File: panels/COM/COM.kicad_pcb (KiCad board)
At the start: 2 copper layers, 71 x 132.5 mm, 4 parts

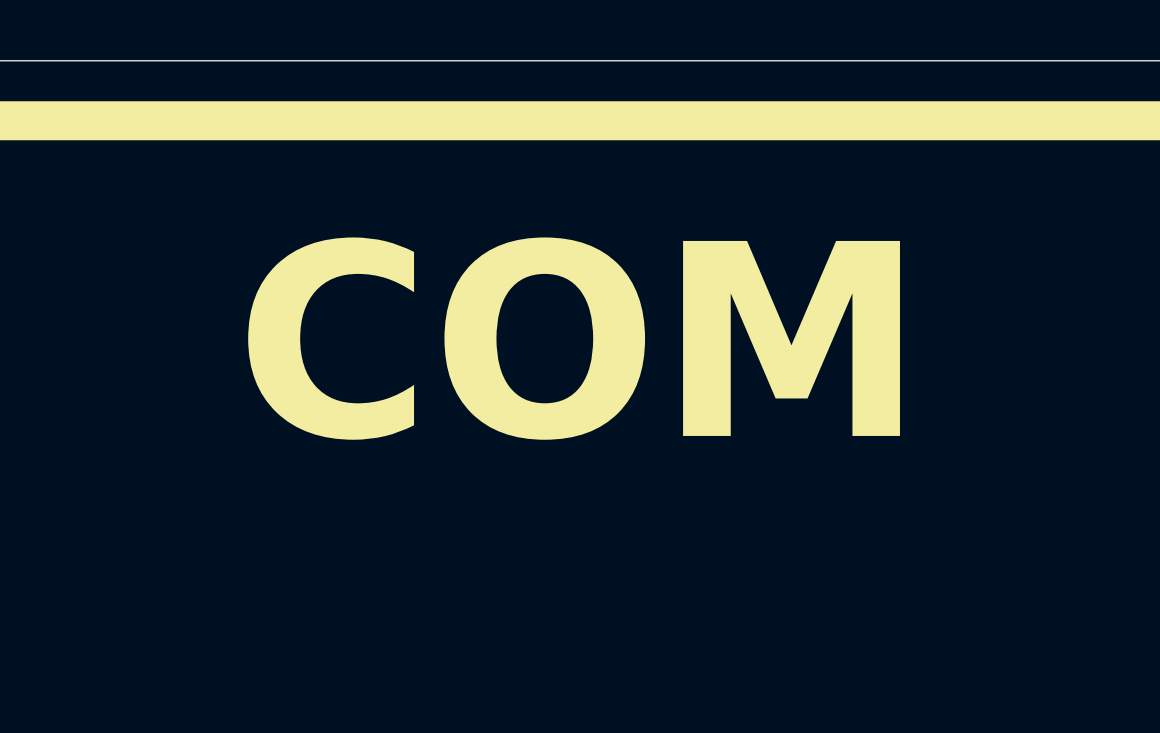
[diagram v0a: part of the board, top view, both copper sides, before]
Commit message: 3U panels initial version
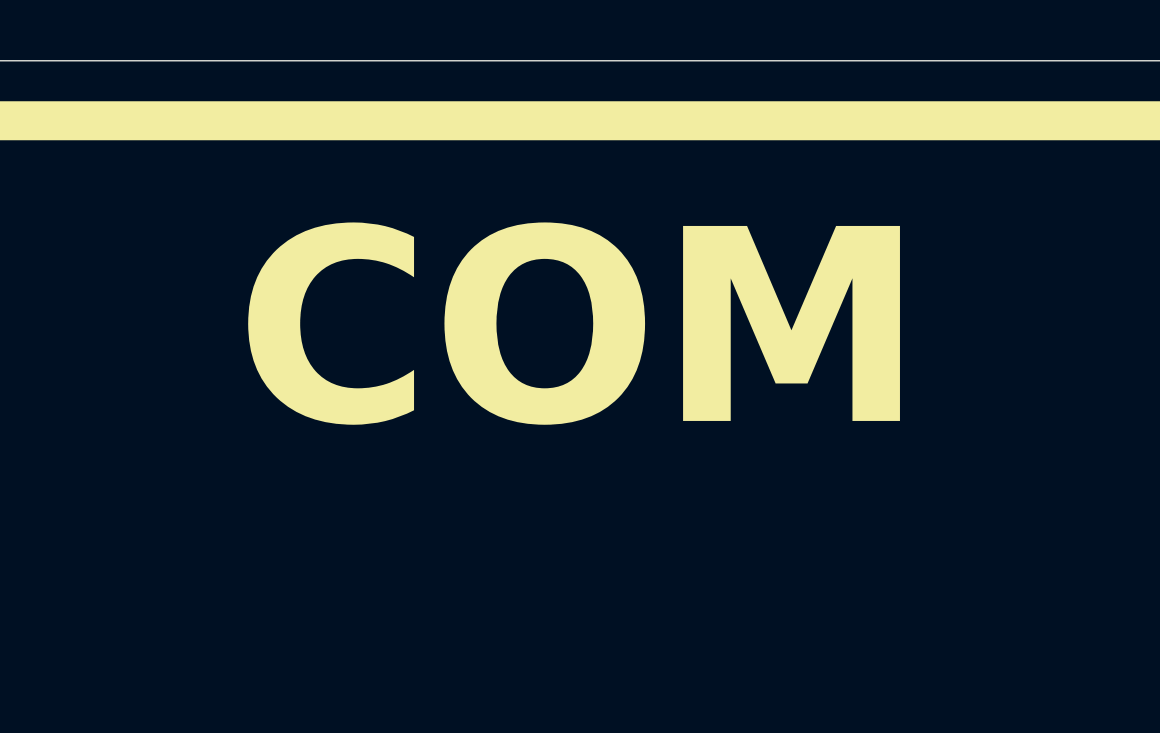
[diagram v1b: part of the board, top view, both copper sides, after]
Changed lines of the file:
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@@
 	)
 	(gr_text "COM"
-		(at 101.745894 44.915428 0)
+		(at 101.745894 44.415428 0)
 		(layer "F.SilkS")
 		(effects
@@
 			(polygon
 				(pts
-					(xy 94.889539 45.566539) (xy 94.851151 46.22562) (xy 94.751219 46.697101) (xy 94.607595 47.025142)
-					(xy 94.429935 47.245403) (xy 94.193747 47.403744) (xy 93.839887 47.53445) (xy 93.329149 47.626331)
-					(xy 92.614539 47.661746) (xy 91.203976 47.689131) (xy 90.057744 47.670874) (xy 89.246857 47.642712)
-					(xy 88.645545 47.56866) (xy 88.211816 47.462466) (xy 87.908803 47.33485) (xy 87.70535 47.192616)
-					(xy 87.488232 46.937991) (xy 87.325718 46.615743) (xy 87.220507 46.210524) (xy 87.182243 45.702277)
-					(xy 87.127471 44.426261) (xy 87.161982 43.648642) (xy 87.25475 43.044425) (xy 87.392067 42.582122)
-					(xy 87.564055 42.234212) (xy 87.754235 42.002544) (xy 88.010959 41.814211) (xy 88.348204 41.668833)
-					(xy 88.785705 41.572453) (xy 89.3477 41.536868) (xy 91.07697 41.491225) (xy 92.323616 41.505116)
-					(xy 93.51549 41.591242) (xy 93.853291 41.660521) (xy 94.125091 41.785758) (xy 94.343688 41.96481)
-					(xy 94.516459 42.202857) (xy 94.673885 42.575213) (xy 94.778324 43.057298) (xy 94.816908 43.675733)
-					(xy 93.024135 43.675733) (xy 92.996554 43.415026) (xy 92.925515 43.243628) (xy 92.819337 43.135162)
-					(xy 92.579763 43.0384) (xy 92.168827 42.998631) (xy 91.650086 42.989899) (xy 91.140473 42.989899)
-					(xy 90.203008 42.999027) (xy 89.761685 43.026373) (xy 89.470175 43.095247) (xy 89.286704 43.190806)
-					(xy 89.179416 43.306621) (xy 89.090478 43.527118) (xy 89.021501 43.924549) (xy 88.992876 44.581049)
-					(xy 89.026534 45.254817) (xy 89.107183 45.655987) (xy 89.211168 45.874132) (xy 89.331661 45.983979)
-					(xy 89.539178 46.077077) (xy 89.871415 46.145078) (xy 90.376054 46.1722) (xy 91.095227 46.190457)
-					(xy 92.041424 46.181329) (xy 92.4127 46.159719) (xy 92.666419 46.104628) (xy 92.833228 46.027333)
-					(xy 92.95155 45.901031) (xy 93.035608 45.675596) (xy 93.069778 45.301413) (xy 94.880411 45.301413)
+					(xy 94.889539 45.066539) (xy 94.851151 45.72562) (xy 94.751219 46.197101) (xy 94.607595 46.525142)
+					(xy 94.429935 46.745403) (xy 94.193747 46.903744) (xy 93.839887 47.03445) (xy 93.329149 47.126331)
+					(xy 92.614539 47.161746) (xy 91.203976 47.189131) (xy 90.057744 47.170874) (xy 89.246857 47.142712)
+					(xy 88.645545 47.06866) (xy 88.211816 46.962466) (xy 87.908803 46.83485) (xy 87.70535 46.692616)
+					(xy 87.488232 46.437991) (xy 87.325718 46.115743) (xy 87.220507 45.710524) (xy 87.182243 45.202277)
+					(xy 87.127471 43.926261) (xy 87.161982 43.148642) (xy 87.25475 42.544425) (xy 87.392067 42.082122)
+					(xy 87.564055 41.734212) (xy 87.754235 41.502544) (xy 88.010959 41.314211) (xy 88.348204 41.168833)
+					(xy 88.785705 41.072453) (xy 89.3477 41.036868) (xy 91.07697 40.991225) (xy 92.323616 41.005116)
+					(xy 93.51549 41.091242) (xy 93.853291 41.160521) (xy 94.125091 41.285758) (xy 94.343688 41.46481)
+					(xy 94.516459 41.702857) (xy 94.673885 42.075213) (xy 94.778324 42.557298) (xy 94.816908 43.175733)
+					(xy 93.024135 43.175733) (xy 92.996554 42.915026) (xy 92.925515 42.743628) (xy 92.819337 42.635162)
+					(xy 92.579763 42.5384) (xy 92.168827 42.498631) (xy 91.650086 42.489899) (xy 91.140473 42.489899)
+					(xy 90.203008 42.499027) (xy 89.761685 42.526373) (xy 89.470175 42.595247) (xy 89.286704 42.690806)
+					(xy 89.179416 42.806621) (xy 89.090478 43.027118) (xy 89.021501 43.424549) (xy 88.992876 44.081049)
+					(xy 89.026534 44.754817) (xy 89.107183 45.155987) (xy 89.211168 45.374132) (xy 89.331661 45.483979)
+					(xy 89.539178 45.577077) (xy 89.871415 45.645078) (xy 90.376054 45.6722) (xy 91.095227 45.690457)
+					(xy 92.041424 45.681329) (xy 92.4127 45.659719) (xy 92.666419 45.604628) (xy 92.833228 45.527333)
+					(xy 92.95155 45.401031) (xy 93.035608 45.175596) (xy 93.069778 44.801413) (xy 94.880411 44.801413)
 				)
 			)
 			(polygon
 				(pts
-					(xy 101.710967 41.500353) (xy 102.40857 41.52936) (xy 102.953832 41.607517) (xy 103.373505 41.723372)
-					(xy 103.691193 41.868347) (xy 103.92683 42.037352) (xy 104.115138 42.255131) (xy 104.275577 42.555451)
-					(xy 104.403766 42.959342) (xy 104.490577 43.492679) (xy 104.522966 44.185346) (xy 104.522966 44.476269)
-					(xy 104.481868 45.483546) (xy 104.375761 46.198966) (xy 104.226571 46.689239) (xy 104.049867 47.011235)
-					(xy 103.8539 47.205766) (xy 103.554125 47.376178) (xy 103.117171 47.516849) (xy 102.501041 47.615072)
-					(xy 101.656593 47.652617) (xy 100.264287 47.680003) (xy 99.681645 47.689131) (xy 98.425871 47.643488)
-					(xy 97.893121 47.608961) (xy 97.454236 47.513031) (xy 97.093231 47.364094) (xy 96.797015 47.166024)
-					(xy 96.558965 46.908539) (xy 96.381204 46.57795) (xy 96.265961 46.157178) (xy 96.223899 45.623295)
-					(xy 96.205642 44.503655) (xy 96.212404 44.3445) (xy 98.071047 44.3445) (xy 98.071047 44.508418)
-					(xy 98.071047 44.753699) (xy 98.100162 45.31796) (xy 98.171611 45.67282) (xy 98.266716 45.881276)
-					(xy 98.376316 45.99203) (xy 98.555134 46.082531) (xy 98.83006 46.146915) (xy 99.235933 46.1722)
-					(xy 100.227772 46.190457) (xy 101.174366 46.181329) (xy 101.701014 46.157483) (xy 102.061605 46.096873)
-					(xy 102.297975 46.013045) (xy 102.434785 45.911721) (xy 102.53991 45.753118) (xy 102.611685 45.518612)
-					(xy 102.639304 45.181154) (xy 102.657561 44.362757) (xy 102.64394 43.959627) (xy 102.607552 43.649141)
-					(xy 102.526466 43.381954) (xy 102.402755 43.212557) (xy 102.222016 43.100353) (xy 101.943151 43.026413)
-					(xy 101.632904 42.99252) (xy 101.29264 42.98077) (xy 99.454225 42.989899) (xy 98.865133 43.026824)
-					(xy 98.498502 43.117302) (xy 98.314208 43.230875) (xy 98.189379 43.405077) (xy 98.121056 43.658269)
-					(xy 98.071047 44.3445) (xy 96.212404 44.3445) (xy 96.247561 43.517056) (xy 96.35475 42.832265)
-					(xy 96.503795 42.376186) (xy 96.67874 42.087361) (xy 96.870705 41.914873) (xy 97.158251 41.763358)
-					(xy 97.571214 41.638506) (xy 98.14637 41.551668) (xy 98.926355 41.518611) (xy 100.236901 41.491225)
+					(xy 101.710967 41.000353) (xy 102.40857 41.02936) (xy 102.953832 41.107517) (xy 103.373505 41.223372)
+					(xy 103.691193 41.368347) (xy 103.92683 41.537352) (xy 104.115138 41.755131) (xy 104.275577 42.055451)
+					(xy 104.403766 42.459342) (xy 104.490577 42.992679) (xy 104.522966 43.685346) (xy 104.522966 43.976269)
+					(xy 104.481868 44.983546) (xy 104.375761 45.698966) (xy 104.226571 46.189239) (xy 104.049867 46.511235)
+					(xy 103.8539 46.705766) (xy 103.554125 46.876178) (xy 103.117171 47.016849) (xy 102.501041 47.115072)
+					(xy 101.656593 47.152617) (xy 100.264287 47.180003) (xy 99.681645 47.189131) (xy 98.425871 47.143488)
+					(xy 97.893121 47.108961) (xy 97.454236 47.013031) (xy 97.093231 46.864094) (xy 96.797015 46.666024)
+					(xy 96.558965 46.408539) (xy 96.381204 46.07795) (xy 96.265961 45.657178) (xy 96.223899 45.123295)
+					(xy 96.205642 44.003655) (xy 96.212404 43.8445) (xy 98.071047 43.8445) (xy 98.071047 44.008418)
+					(xy 98.071047 44.253699) (xy 98.100162 44.81796) (xy 98.171611 45.17282) (xy 98.266716 45.381276)
+					(xy 98.376316 45.49203) (xy 98.555134 45.582531) (xy 98.83006 45.646915) (xy 99.235933 45.6722)
+					(xy 100.227772 45.690457) (xy 101.174366 45.681329) (xy 101.701014 45.657483) (xy 102.061605 45.596873)
+					(xy 102.297975 45.513045) (xy 102.434785 45.411721) (xy 102.53991 45.253118) (xy 102.611685 45.018612)
+					(xy 102.639304 44.681154) (xy 102.657561 43.862757) (xy 102.64394 43.459627) (xy 102.607552 43.149141)
+					(xy 102.526466 42.881954) (xy 102.402755 42.712557) (xy 102.222016 42.600353) (xy 101.943151 42.526413)
+					(xy 101.632904 42.49252) (xy 101.29264 42.48077) (xy 99.454225 42.489899) (xy 98.865133 42.526824)
+					(xy 98.498502 42.617302) (xy 98.314208 42.730875) (xy 98.189379 42.905077) (xy 98.121056 43.158269)
+					(xy 98.071047 43.8445) (xy 96.212404 43.8445) (xy 96.247561 43.017056) (xy 96.35475 42.332265)
+					(xy 96.503795 41.876186) (xy 96.67874 41.587361) (xy 96.870705 41.414873) (xy 97.158251 41.263358)
+					(xy 97.571214 41.138506) (xy 98.14637 41.051668) (xy 98.926355 41.018611) (xy 100.236901 40.991225)
 				)
 			)
 			(polygon
 				(pts
-					(xy 114.51201 47.638329) (xy 114.51201 43.015697) (xy 111.836543 47.638329) (xy 110.353348 47.638329)
-					(xy 107.705267 43.015697) (xy 107.705267 47.638329) (xy 105.967265 47.638329) (xy 105.967265 41.516626)
-					(xy 108.906667 41.516626) (xy 111.136024 45.549869) (xy 113.337996 41.516626) (xy 116.25914 41.516626)
-					(xy 116.25914 47.638329)
+					(xy 114.51201 47.138329) (xy 114.51201 42.515697) (xy 111.836543 47.138329) (xy 110.353348 47.138329)
+					(xy 107.705267 42.515697) (xy 107.705267 47.138329) (xy 105.967265 47.138329) (xy 105.967265 41.016626)
+					(xy 108.906667 41.016626) (xy 111.136024 45.049869) (xy 113.337996 41.016626) (xy 116.25914 41.016626)
+					(xy 116.25914 47.138329)
 				)
 			)

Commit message: panel dials, leds, jacks and pcb brackets
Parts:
- added Dial_Scale**: Dial_0_9, FormantKO-Panel:Dial_0_9, F.Cu at (118.7, 66.4)
- added Dial_Scale**: Dial_0_9, FormantKO-Panel:Dial_0_9, F.Cu at (84.7, 66.4)
- added Dial_Scale**: Dial_0_9, FormantKO-Panel:Dial_0_9, F.Cu at (84.7, 101.4)
- added Dial_Scale**: Dial_0_9, FormantKO-Panel:Dial_0_9, F.Cu at (118.7, 101.4)
- added REF**: Jack_3.5mm, FormantKO-Panel:Jack_3.5mm, F.Cu at (84.7, 136.4)
- added REF**: LED_5mm_Small_Bezel, FormantKO-Panel:LED_5mm_Small_Bezel, F.Cu at (84.7, 121.4)
- added REF**: LED_5mm_Small_Bezel, FormantKO-Panel:LED_5mm_Small_Bezel, F.Cu at (118.7, 121.4)
- added REF**: LED_5mm_Small_Bezel, FormantKO-Panel:LED_5mm_Small_Bezel, F.Cu at (101.7, 121.4)
- added REF**: LED_5mm_Small_Bezel, FormantKO-Panel:LED_5mm_Small_Bezel, F.Cu at (101.7, 81.4)
- added REF**: Jack_3.5mm, FormantKO-Panel:Jack_3.5mm, F.Cu at (118.7, 136.4)
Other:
- outline, holes or cut-outs redrawn

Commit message: additional panel work
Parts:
- added H5: MountingHole, MountingHole:MountingHole_2.7mm_M2.5, F.Cu at (101.5, 49.6)
- added H6: MountingHole, MountingHole:MountingHole_2.7mm_M2.5, F.Cu at (101.5, 149.6)
- moved H1 2.67 mm to (73.7, 39.4)
- moved H2 2.67 mm to (129.8, 39.4)
- moved H3 2.67 mm to (73.7, 163.9)
- moved H4 2.67 mm to (129.8, 163.9)
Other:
- board text added: "FORMANT^{KO}"
- board text added: "| ${COMPANY} | ${COMMENT1} ${TITLE} | REVISION ${REVISION} | ${ISSUE_DATE} |"
- board text added: "| ${EMAIL} | ${GITHUB} |"
